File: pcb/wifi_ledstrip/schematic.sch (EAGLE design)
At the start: 65 parts, among them IC1 STM32F10XCXT6, Q1 8MHz

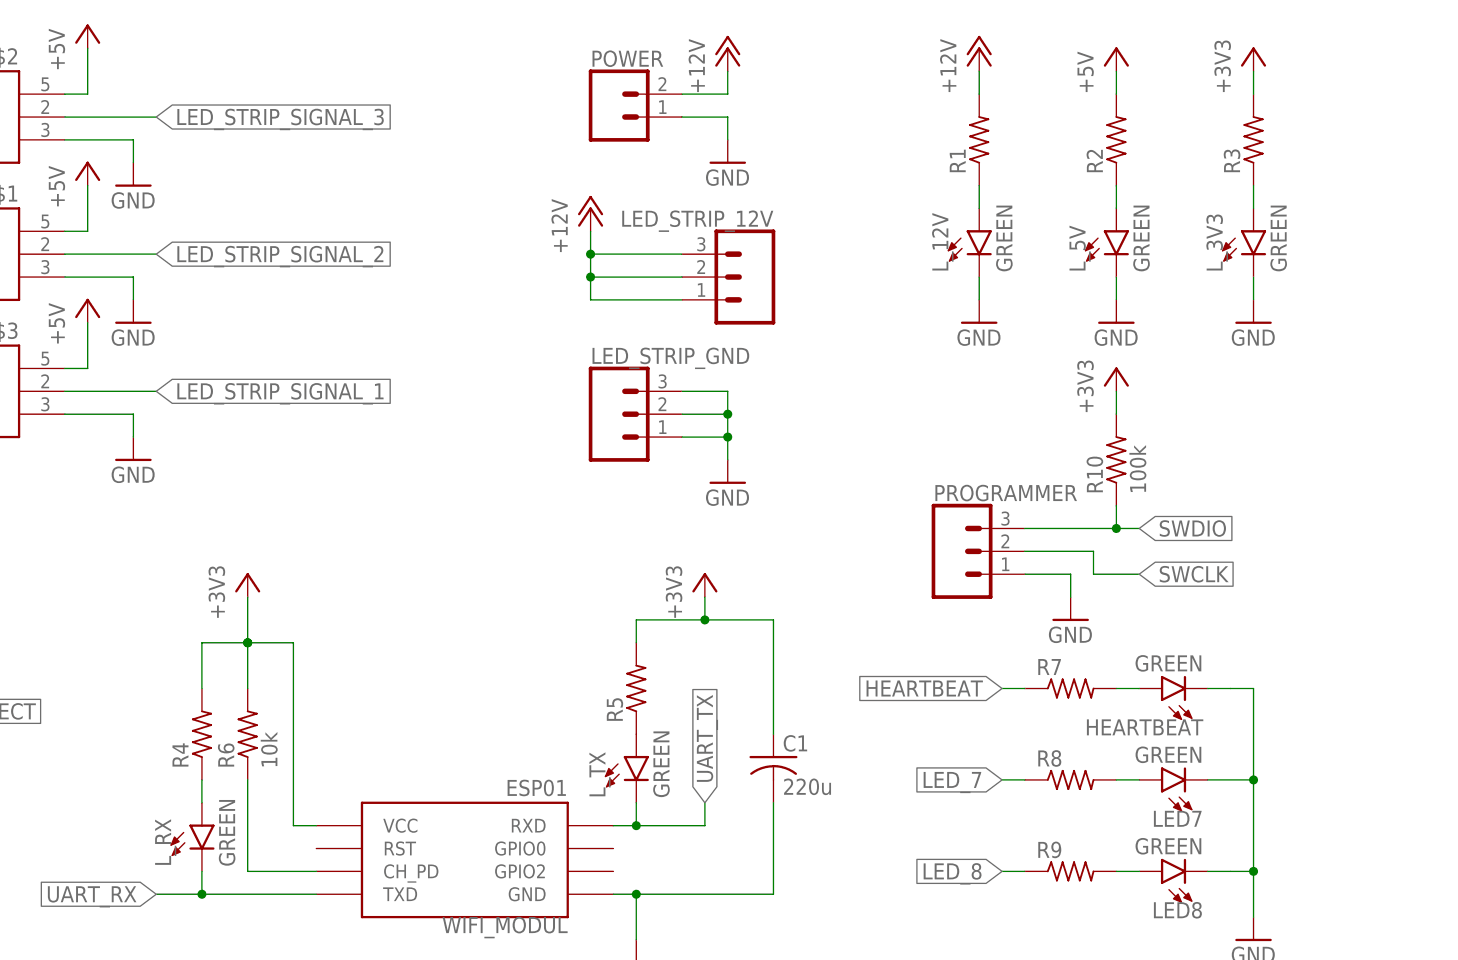
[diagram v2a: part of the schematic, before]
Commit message: pcb updated with leds
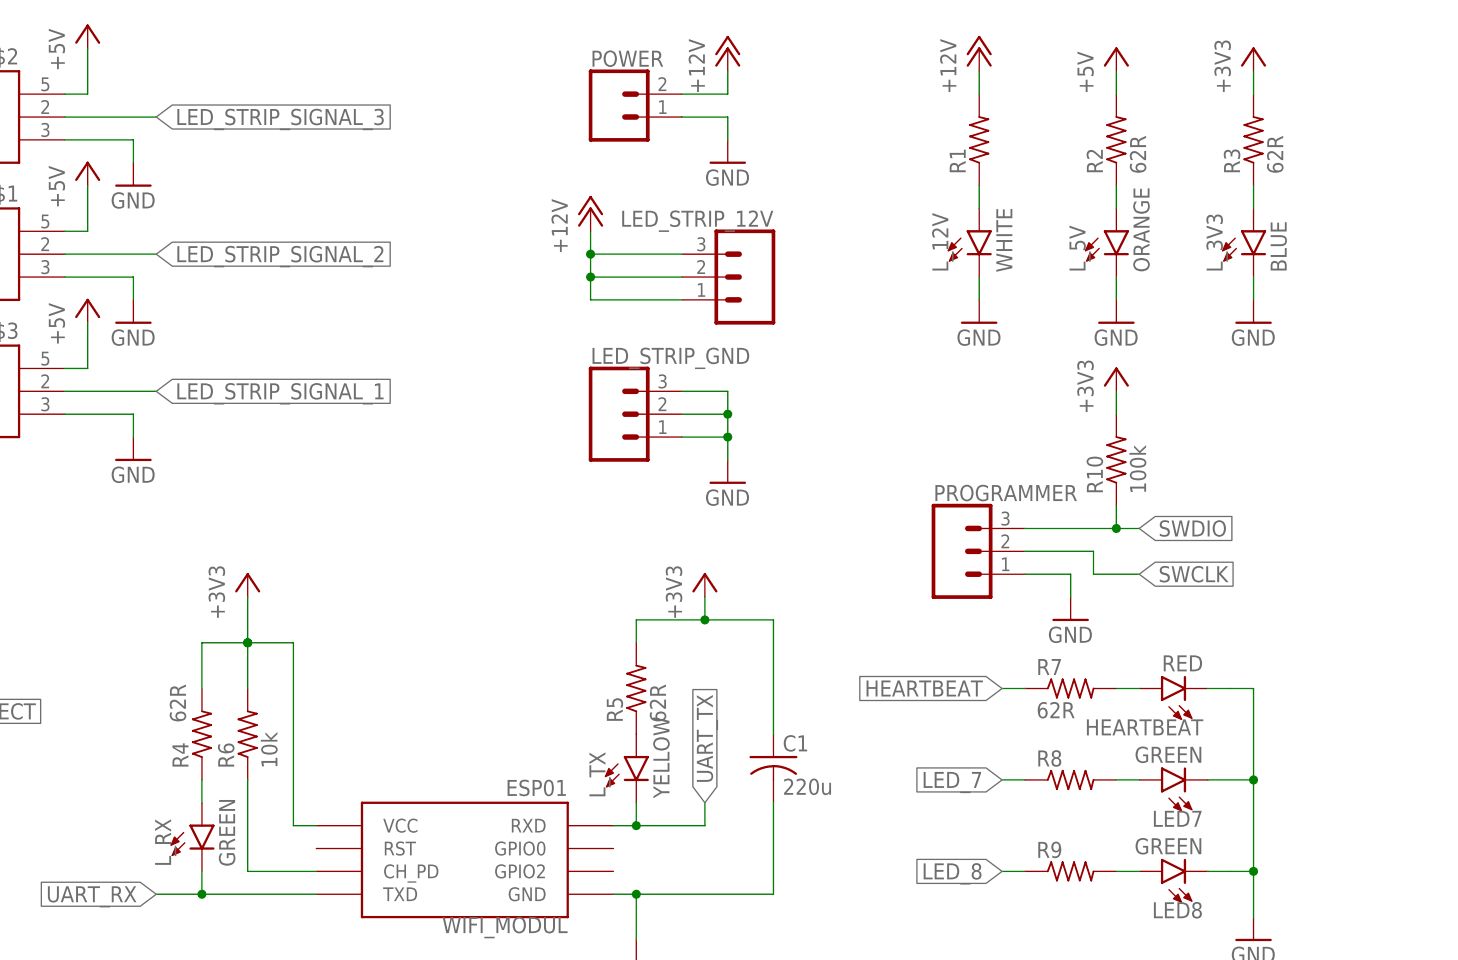
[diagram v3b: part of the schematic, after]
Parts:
- HEARTBEAT: value GREEN -> RED
- L_12V: value GREEN -> WHITE
- L_3V3: value GREEN -> BLUE
- L_5V: value GREEN -> ORANGE
- L_TX: value GREEN -> YELLOW
- R2, R3, R4, R5, R7: value (none) -> 62R
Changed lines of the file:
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@@
 <part name="SW_4" library="mylibrary" deviceset="TACTILE_SWITCH_SIDE" device="TACTILE_SWITCH_SIDE"/>
 <part name="POWER" library="SparkFun-Connectors" library_urn="urn:adsk.eagle:library:513" deviceset="CONN_02" device="5MM" package3d_urn="urn:adsk.eagle:package:38044/1"/>
-<part name="L_12V" library="SparkFun-LED" library_urn="urn:adsk.eagle:library:529" deviceset="LED-GREEN" device="1206" package3d_urn="urn:adsk.eagle:package:39352/1" value="GREEN"/>
-<part name="L_5V" library="SparkFun-LED" library_urn="urn:adsk.eagle:library:529" deviceset="LED-GREEN" device="1206" package3d_urn="urn:adsk.eagle:package:39352/1" value="GREEN"/>
-<part name="L_3V3" library="SparkFun-LED" library_urn="urn:adsk.eagle:library:529" deviceset="LED-GREEN" device="1206" package3d_urn="urn:adsk.eagle:package:39352/1" value="GREEN"/>
+<part name="L_12V" library="SparkFun-LED" library_urn="urn:adsk.eagle:library:529" deviceset="LED-GREEN" device="1206" package3d_urn="urn:adsk.eagle:package:39352/1" value="WHITE"/>
+<part name="L_5V" library="SparkFun-LED" library_urn="urn:adsk.eagle:library:529" deviceset="LED-GREEN" device="1206" package3d_urn="urn:adsk.eagle:package:39352/1" value="ORANGE"/>
+<part name="L_3V3" library="SparkFun-LED" library_urn="urn:adsk.eagle:library:529" deviceset="LED-GREEN" device="1206" package3d_urn="urn:adsk.eagle:package:39352/1" value="BLUE"/>
 <part name="L_RX" library="SparkFun-LED" library_urn="urn:adsk.eagle:library:529" deviceset="LED-GREEN" device="1206" package3d_urn="urn:adsk.eagle:package:39352/1" value="GREEN"/>
-<part name="L_TX" library="SparkFun-LED" library_urn="urn:adsk.eagle:library:529" deviceset="LED-GREEN" device="1206" package3d_urn="urn:adsk.eagle:package:39352/1" value="GREEN"/>
-<part name="HEARTBEAT" library="SparkFun-LED" library_urn="urn:adsk.eagle:library:529" deviceset="LED-GREEN" device="1206" package3d_urn="urn:adsk.eagle:package:39352/1" value="GREEN"/>
+<part name="L_TX" library="SparkFun-LED" library_urn="urn:adsk.eagle:library:529" deviceset="LED-GREEN" device="1206" package3d_urn="urn:adsk.eagle:package:39352/1" value="YELLOW"/>
+<part name="HEARTBEAT" library="SparkFun-LED" library_urn="urn:adsk.eagle:library:529" deviceset="LED-GREEN" device="1206" package3d_urn="urn:adsk.eagle:package:39352/1" value="RED"/>
 <part name="LED7" library="SparkFun-LED" library_urn="urn:adsk.eagle:library:529" deviceset="LED-GREEN" device="1206" package3d_urn="urn:adsk.eagle:package:39352/1" value="GREEN"/>
 <part name="LED8" library="SparkFun-LED" library_urn="urn:adsk.eagle:library:529" deviceset="LED-GREEN" device="1206" package3d_urn="urn:adsk.eagle:package:39352/1" value="GREEN"/>
@@
 <part name="GND6" library="supply1" library_urn="urn:adsk.eagle:library:371" deviceset="GND" device=""/>
 <part name="R1" library="rcl" library_urn="urn:adsk.eagle:library:334" deviceset="R-US_" device="R1206" package3d_urn="urn:adsk.eagle:package:23540/2"/>
-<part name="R2" library="rcl" library_urn="urn:adsk.eagle:library:334" deviceset="R-US_" device="R1206" package3d_urn="urn:adsk.eagle:package:23540/2"/>
-<part name="R3" library="rcl" library_urn="urn:adsk.eagle:library:334" deviceset="R-US_" device="R1206" package3d_urn="urn:adsk.eagle:package:23540/2"/>
+<part name="R2" library="rcl" library_urn="urn:adsk.eagle:library:334" deviceset="R-US_" device="R1206" package3d_urn="urn:adsk.eagle:package:23540/2" value="62R"/>
+<part name="R3" library="rcl" library_urn="urn:adsk.eagle:library:334" deviceset="R-US_" device="R1206" package3d_urn="urn:adsk.eagle:package:23540/2" value="62R"/>
 <part name="GND7" library="supply1" library_urn="urn:adsk.eagle:library:371" deviceset="GND" device=""/>
 <part name="GND8" library="supply1" library_urn="urn:adsk.eagle:library:371" deviceset="GND" device=""/>
 <part name="GND9" library="supply1" library_urn="urn:adsk.eagle:library:371" deviceset="GND" device=""/>
 <part name="GND10" library="supply1" library_urn="urn:adsk.eagle:library:371" deviceset="GND" device=""/>
-<part name="R4" library="rcl" library_urn="urn:adsk.eagle:library:334" deviceset="R-US_" device="R1206" package3d_urn="urn:adsk.eagle:package:23540/2"/>
-<part name="R5" library="rcl" library_urn="urn:adsk.eagle:library:334" deviceset="R-US_" device="R1206" package3d_urn="urn:adsk.eagle:package:23540/2"/>
+<part name="R4" library="rcl" library_urn="urn:adsk.eagle:library:334" deviceset="R-US_" device="R1206" package3d_urn="urn:adsk.eagle:package:23540/2" value="62R"/>
+<part name="R5" library="rcl" library_urn="urn:adsk.eagle:library:334" deviceset="R-US_" device="R1206" package3d_urn="urn:adsk.eagle:package:23540/2" value="62R"/>
 <part name="R6" library="rcl" library_urn="urn:adsk.eagle:library:334" deviceset="R-US_" device="R1206" package3d_urn="urn:adsk.eagle:package:23540/2" value="10k"/>
 <part name="C1" library="rcl" library_urn="urn:adsk.eagle:library:334" deviceset="C-US" device="C1206" package3d_urn="urn:adsk.eagle:package:23618/2" value="220u"/>
-<part name="R7" library="rcl" library_urn="urn:adsk.eagle:library:334" deviceset="R-US_" device="R1206" package3d_urn="urn:adsk.eagle:package:23540/2"/>
+<part name="R7" library="rcl" library_urn="urn:adsk.eagle:library:334" deviceset="R-US_" device="R1206" package3d_urn="urn:adsk.eagle:package:23540/2" value="62R"/>
 <part name="R8" library="rcl" library_urn="urn:adsk.eagle:library:334" deviceset="R-US_" device="R1206" package3d_urn="urn:adsk.eagle:package:23540/2"/>
 <part name="R9" library="rcl" library_urn="urn:adsk.eagle:library:334" deviceset="R-US_" device="R1206" package3d_urn="urn:adsk.eagle:package:23540/2"/>
@@
 <instance part="R4" gate="G$1" x="88.9" y="15.24" smashed="yes" rot="R90">
 <attribute name="NAME" x="87.4014" y="11.43" size="1.778" layer="95" rot="R90"/>
-<attribute name="VALUE" x="92.202" y="11.43" size="1.778" layer="96" rot="R90"/>
+<attribute name="VALUE" x="87.122" y="16.51" size="1.778" layer="96" rot="R90"/>
 </instance>
 <instance part="R5" gate="G$1" x="137.16" y="20.32" smashed="yes" rot="R90">
